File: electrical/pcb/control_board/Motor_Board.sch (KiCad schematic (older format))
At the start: 83 parts, among them J1 XT30-M, J10 Molex_172675-0613, J11 Molex_172675-0613, J12 TSW-104-07-F-T, J13 Molex_172675-0613, J14 Molex_172675-0613, J15 TSW-104-07-F-T, J16 277-11404-ND, J17 277-11404-ND, J18 277-11404-ND, J19 TSW-104-07-F-T, J2 XT30-F, J20 PEC08SAAN, J21 PPTC102LFBN-RC, J3 XT30-F, J4 XT30-F, J5 XT30-M, J6 ED2580-ND, J7 TSW-104-07-F-T, J8 Molex_172675-0613, J9 Molex_172675-0613, T1 test_point, T10 JPL Robotics:test_point_hole, T11 JPL Robotics:test_point_hole, T12 JPL Robotics:test_point_hole, T2 test_point, T3 JPL Robotics:test_point, T4 JPL Robotics:test_point, T5 JPL Robotics:test_point, T6 test_point, T7 test_point, T8 JPL Robotics:test_point_hole, T9 JPL Robotics:test_point_hole, U1 INA260, U2 PCA9685, U3 D24V22Fx, U4 D24V150Fx, U5 DC7G3HWA, y1 rover_silkscreen

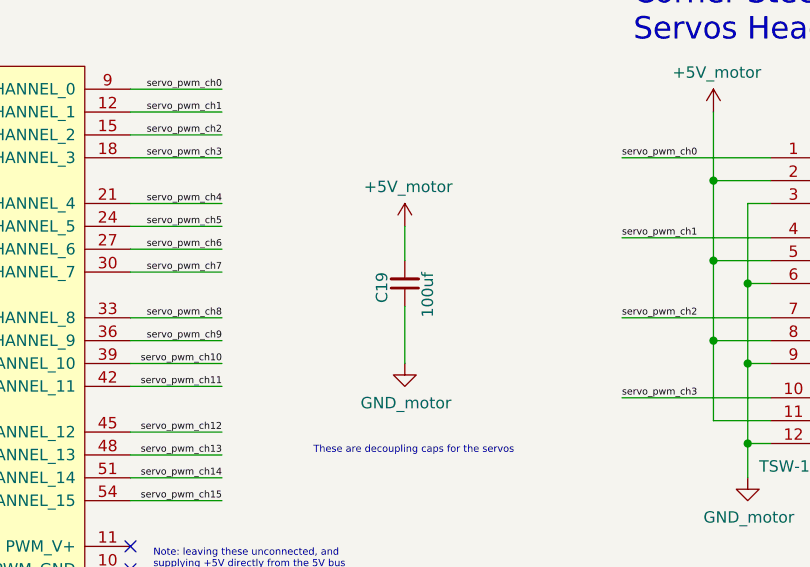
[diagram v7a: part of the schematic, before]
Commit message: Touching up 3d models for j24, LED arrays, c19
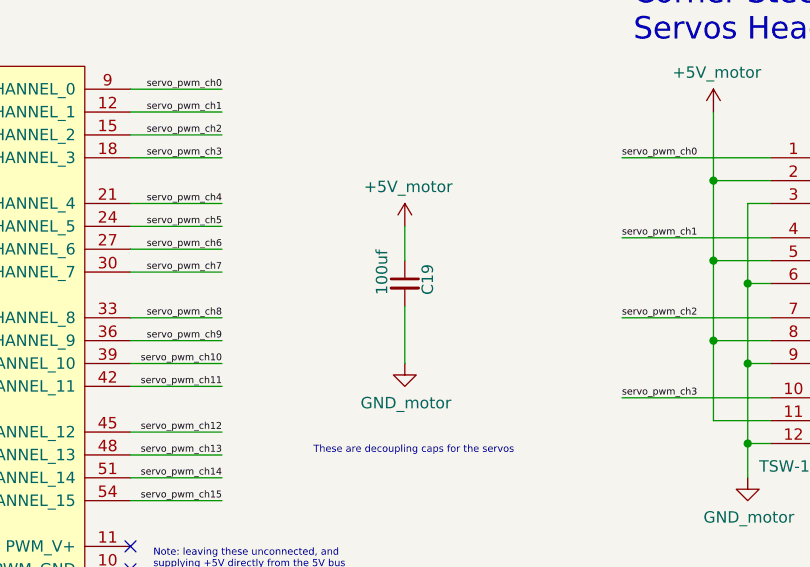
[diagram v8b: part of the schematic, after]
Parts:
- T10, T11, T12, T8, T9: value JPL Robotics:test_point_hole -> test_point; footprint (none) -> JPL Robotics:test_point_hole
- T3, T4, T5: value JPL Robotics:test_point -> test_point; footprint (none) -> JPL Robotics:test_point
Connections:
- net +5V_motor: now also C19.1; no longer C19.2
- net GND_motor: now also C19.2; no longer C19.1
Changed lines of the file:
@@
 F 3 "~" H 9300 6300 50  0001 C CNN
 	1    9300 6300
-	-1   0    0    1
+	1    0    0    -1
 $EndComp
 $Comp
@@
 P 3750 9550
 F 0 "T8" V 3800 9500 50  0000 L TNN
-F 1 "JPL Robotics:test_point_hole" H 3900 9800 50  0001 C CNN
-F 2 "" H 3700 9500 50  0001 C CNN
+F 1 "test_point" H 3900 9800 50  0001 C CNN
+F 2 "JPL Robotics:test_point_hole" H 3700 9500 50  0001 C CNN
 F 3 "" H 3700 9500 50  0001 C CNN
 	1    3750 9550
@@
 P 3900 9550
 F 0 "T9" V 3950 9500 50  0000 L TNN
-F 1 "JPL Robotics:test_point_hole" H 4050 9800 50  0001 C CNN
-F 2 "" H 3850 9500 50  0001 C CNN
+F 1 "test_point" H 4050 9800 50  0001 C CNN
+F 2 "JPL Robotics:test_point_hole" H 3850 9500 50  0001 C CNN
 F 3 "" H 3850 9500 50  0001 C CNN
 	1    3900 9550
@@
 P 4100 9550
 F 0 "T10" V 4150 9500 50  0000 L TNN
-F 1 "JPL Robotics:test_point_hole" H 4250 9800 50  0001 C CNN
-F 2 "" H 4050 9500 50  0001 C CNN
+F 1 "test_point" H 4250 9800 50  0001 C CNN
+F 2 "JPL Robotics:test_point_hole" H 4050 9500 50  0001 C CNN
 F 3 "" H 4050 9500 50  0001 C CNN
 	1    4100 9550
-	0    -1   -1   0
-$EndComp
-$Comp
-L JPL_Robotics_Lib:test_point T11
-U 1 1 6418FAFC
-P 4300 9550
-F 0 "T11" V 4350 9500 50  0000 L TNN
-F 1 "JPL Robotics:test_point_hole" H 4450 9800 50  0001 C CNN
-F 2 "" H 4250 9500 50  0001 C CNN
-F 3 "" H 4250 9500 50  0001 C CNN
-	1    4300 9550
 	0    -1   -1   0
 $EndComp
@@
 P 2050 5500
 F 0 "T3" V 2100 5450 50  0000 L TNN
-F 1 "JPL Robotics:test_point" H 2200 5750 50  0001 C CNN
-F 2 "" H 2000 5450 50  0001 C CNN
+F 1 "test_point" H 2200 5750 50  0001 C CNN
+F 2 "JPL Robotics:test_point" H 2000 5450 50  0001 C CNN
 F 3 "" H 2000 5450 50  0001 C CNN
 	1    2050 5500
@@
 P 2600 5500
 F 0 "T4" V 2650 5450 50  0000 L TNN
-F 1 "JPL Robotics:test_point" H 2750 5750 50  0001 C CNN
-F 2 "" H 2550 5450 50  0001 C CNN
+F 1 "test_point" H 2750 5750 50  0001 C CNN
+F 2 "JPL Robotics:test_point" H 2550 5450 50  0001 C CNN
 F 3 "" H 2550 5450 50  0001 C CNN
 	1    2600 5500
@@
 P 3550 5500
 F 0 "T5" V 3600 5450 50  0000 L TNN
-F 1 "JPL Robotics:test_point" H 3700 5750 50  0001 C CNN
-F 2 "" H 3500 5450 50  0001 C CNN
+F 1 "test_point" H 3700 5750 50  0001 C CNN
+F 2 "JPL Robotics:test_point" H 3500 5450 50  0001 C CNN
 F 3 "" H 3500 5450 50  0001 C CNN
 	1    3550 5500
@@
 P 4500 9550
 F 0 "T12" V 4550 9500 50  0000 L TNN
-F 1 "JPL Robotics:test_point_hole" H 4650 9800 50  0001 C CNN
-F 2 "" H 4450 9500 50  0001 C CNN
+F 1 "test_point" H 4650 9800 50  0001 C CNN
+F 2 "JPL Robotics:test_point_hole" H 4450 9500 50  0001 C CNN
 F 3 "" H 4450 9500 50  0001 C CNN
 	1    4500 9550
 	0    -1   -1   0
 $EndComp
+$Comp
+L JPL_Robotics_Lib:test_point T11
+U 1 1 6418FAFC
+P 4300 9550
+F 0 "T11" V 4350 9500 50  0000 L TNN
+F 1 "test_point" H 4450 9800 50  0001 C CNN
+F 2 "JPL Robotics:test_point_hole" H 4250 9500 50  0001 C CNN
+F 3 "" H 4250 9500 50  0001 C CNN
+	1    4300 9550
+	0    -1   -1   0
+$EndComp
